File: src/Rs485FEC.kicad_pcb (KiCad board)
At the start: 2 copper layers, 24 x 27.9 mm, 20 parts, among them J1 B4B-XH-A, P1 105444-0001, Q1 DMP3099L-13, U1 FT232RL, U2 SP485E

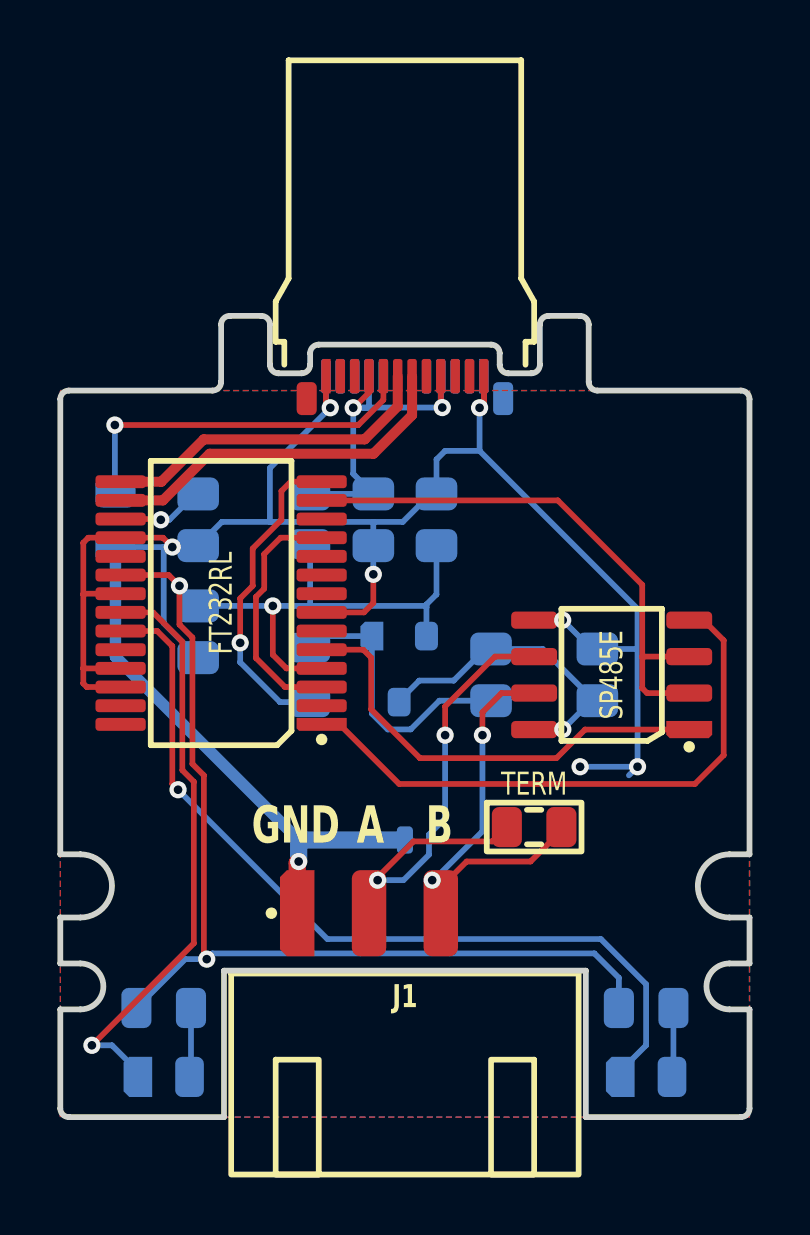
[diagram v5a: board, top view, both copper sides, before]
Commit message: Added PWREN pullup and moved LED 5V to switched
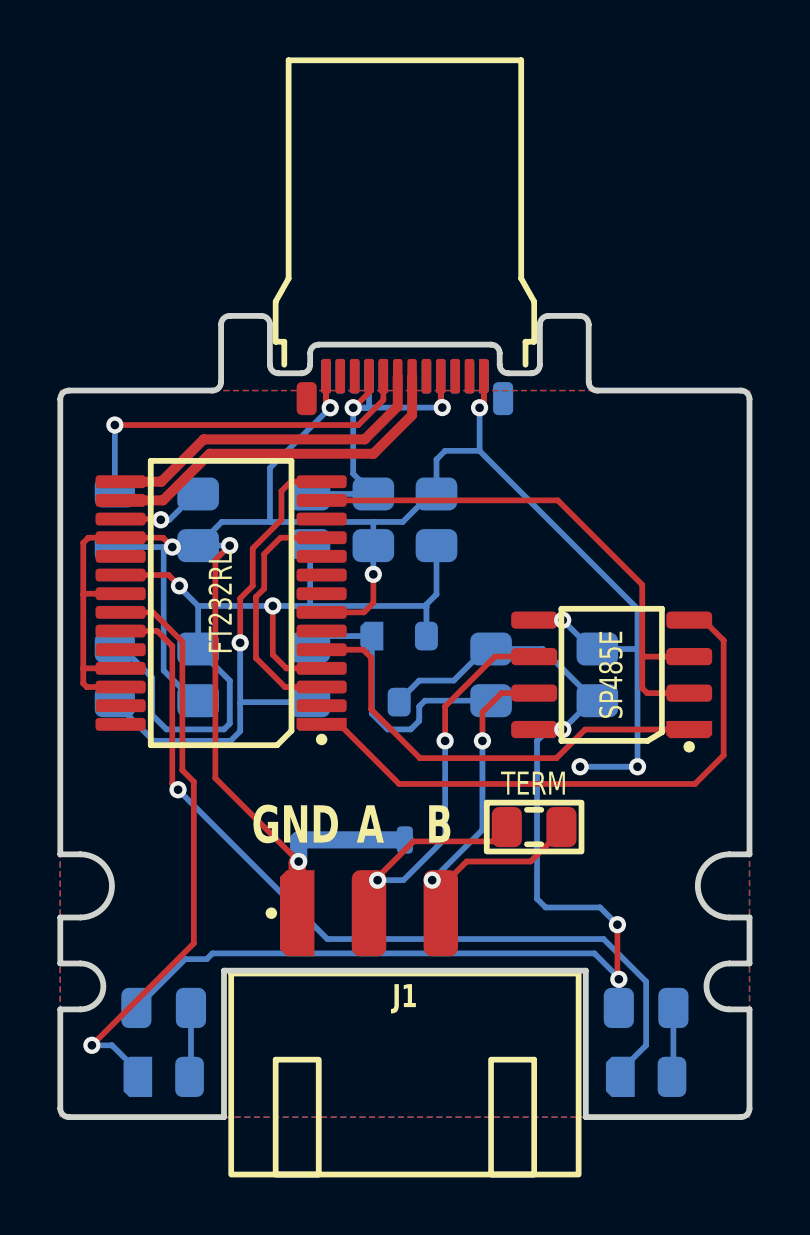
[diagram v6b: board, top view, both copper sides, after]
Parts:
- added R6: 10K, Medo64:R (0805), B.Cu at (21.9, 32.5)
- moved C2 1.50 mm to (24.8, 32.5)
- renumbered R4 to R2, R5 to R3, R6 to R4, R7 to R5
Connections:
- R2 pad 1: 5V -> 5V_SW
- R3 pad 1: 5V -> 5V_SW
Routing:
- net 5V_SW: track 10.2 -> 40.9 mm, vias 1 -> 3
- net 5V: track 52.6 -> 30.5 mm, vias 3 -> 2
- net PWREN#: track 11.3 -> 18.0 mm
- net GND: track 87.5 -> 89.2 mm, vias 8 -> 9

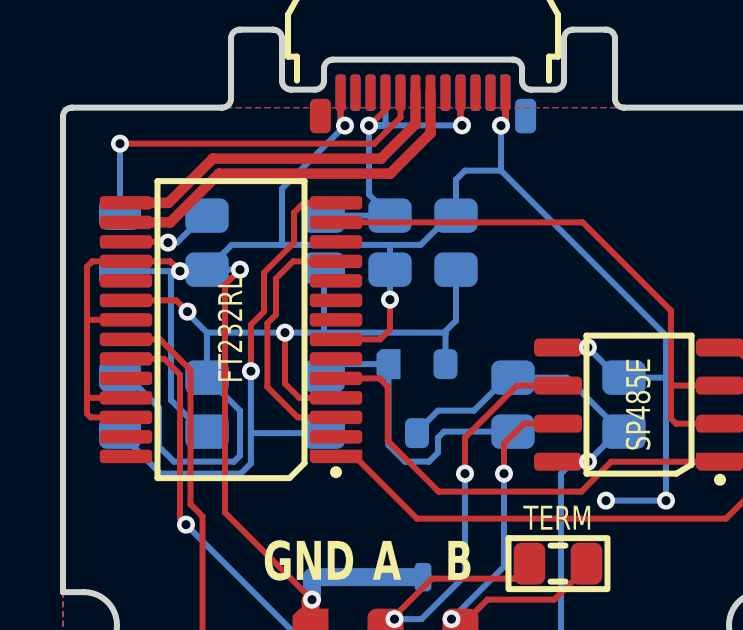
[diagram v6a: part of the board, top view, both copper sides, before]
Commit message: Removed internal RTS/CTS connection
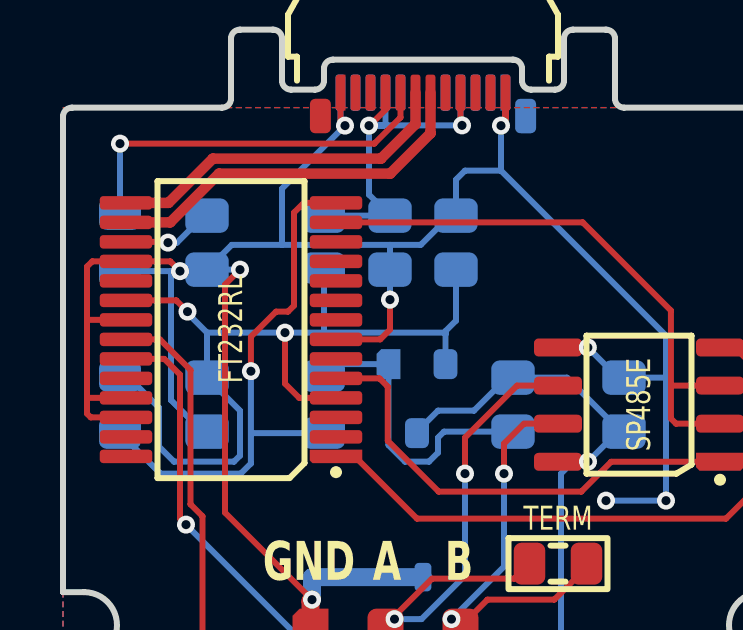
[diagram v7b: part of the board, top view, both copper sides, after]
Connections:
- U1 pad 11: RTS_CTS -> (no net)
- U1 pad 3: RTS_CTS -> (no net)
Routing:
- net RTS_CTS: track 8.68 -> 0.00 mm
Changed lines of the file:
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@@
   (net 18 "B")
   (net 19 "TXDEN")
-  (net 20 "RTS_CTS")
   (footprint "Medo64:R (0805)" (layer "F.Cu")
     (at 36.5 37.8)
@@
       (thermal_bridge_angle 45))
     (pad "3" smd roundrect (at -3.5 -2.925 180) (size 1.75 0.45) (layers "F.Cu" "F.Paste" "F.Mask") (roundrect_rratio 0.25)
-      (net 20 "RTS_CTS") (thermal_bridge_angle 45))
+      (thermal_bridge_angle 45))
     (pad "4" smd roundrect (at -3.5 -2.275 180) (size 1.75 0.45) (layers "F.Cu" "F.Paste" "F.Mask") (roundrect_rratio 0.25)
       (net 3 "5V") (thermal_bridge_angle 45))
@@
       (thermal_bridge_angle 45))
     (pad "11" smd roundrect (at -3.5 2.275 180) (size 1.75 0.45) (layers "F.Cu" "F.Paste" "F.Mask") (roundrect_rratio 0.25)
-      (net 20 "RTS_CTS") (thermal_bridge_angle 45))
+      (thermal_bridge_angle 45))
     (pad "12" smd roundrect (at -3.5 2.925 180) (size 1.75 0.45) (layers "F.Cu" "F.Paste" "F.Mask") (roundrect_rratio 0.25)
       (thermal_bridge_angle 45))
@@
   (segment (start 30.85 31.15) (end 30.85 33.85) (width 0.2) (layer "B.Cu") (net 15))
   (segment (start 32.5 33.6) (end 32.7 33.4) (width 0.2) (layer "B.Cu") (net 15))
-  (segment (start 26.7 28.1) (end 26.7 29.4) (width 0.2) (layer "F.Cu") (net 16))
-  (segment (start 27.7 27.1) (end 26.7 28.1) (width 0.2) (layer "F.Cu") (net 16))
-  (segment (start 27.7 26.1) (end 27.7 27.1) (width 0.2) (layer "F.Cu") (net 16))
+  (segment (start 27.7 29.2) (end 27.5 29.4) (width 0.2) (layer "F.Cu") (net 16))
+  (segment (start 27.1 29.4) (end 26.263909 30.236091) (width 0.2) (layer "F.Cu") (net 16))
+  (segment (start 27.5 29.4) (end 27.1 29.4) (width 0.2) (layer "F.Cu") (net 16))
   (segment (start 29.1 25.775) (end 28.025 25.775) (width 0.2) (layer "F.Cu") (net 16))
-  (segment (start 26.263909 29.836091) (end 26.263909 31.386091) (width 0.2) (layer "F.Cu") (net 16))
+  (segment (start 27.7 26.1) (end 27.7 29.2) (width 0.2) (layer "F.Cu") (net 16))
   (segment (start 28.025 25.775) (end 27.7 26.1) (width 0.2) (layer "F.Cu") (net 16))
-  (segment (start 26.7 29.4) (end 26.263909 29.836091) (width 0.2) (layer "F.Cu") (net 16))
+  (segment (start 26.263909 30.236091) (end 26.263909 31.386091) (width 0.2) (layer "F.Cu") (net 16))
   (via (at 26.263909 31.386091) (size 0.6) (drill 0.3) (layers "F.Cu" "B.Cu") (net 16))
   (segment (start 25.927818 34.8) (end 26.263909 34.463909) (width 0.2) (layer "B.Cu") (net 16))
@@
   (segment (start 29.1 26.425) (end 37.325 26.425) (width 0.2) (layer "F.Cu") (net 19))
   (segment (start 40.435 33.135) (end 40.265 32.965) (width 0.2) (layer "F.Cu") (net 19))
-  (segment (start 27.825 32.925) (end 26.813909 31.913909) (width 0.2) (layer "F.Cu") (net 20))
-  (segment (start 26.813909 29.786091) (end 27.1 29.5) (width 0.2) (layer "F.Cu") (net 20))
-  (segment (start 27.669974 27.725) (end 29.1 27.725) (width 0.2) (layer "F.Cu") (net 20))
-  (segment (start 27.1 28.294974) (end 27.669974 27.725) (width 0.2) (layer "F.Cu") (net 20))
-  (segment (start 29.1 32.925) (end 27.825 32.925) (width 0.2) (layer "F.Cu") (net 20))
-  (segment (start 26.813909 31.913909) (end 26.813909 29.786091) (width 0.2) (layer "F.Cu") (net 20))
-  (segment (start 27.1 29.5) (end 27.1 28.294974) (width 0.2) (layer "F.Cu") (net 20))
   (zone (net 7) (net_name "GND") (layers "F&B.Cu") (hatch edge 0.5)
     (connect_pads (clearance 0.2))

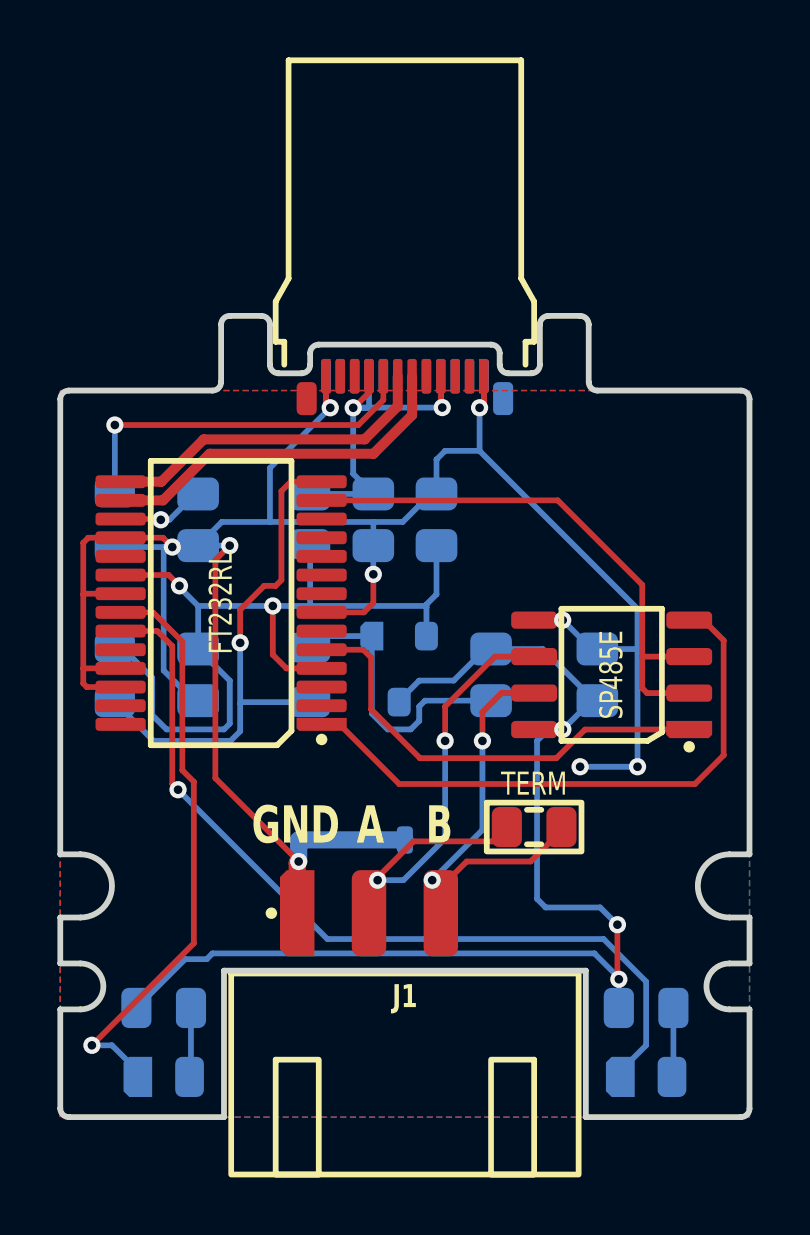
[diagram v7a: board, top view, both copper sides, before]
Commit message: Updated connector to solder all 4 pins
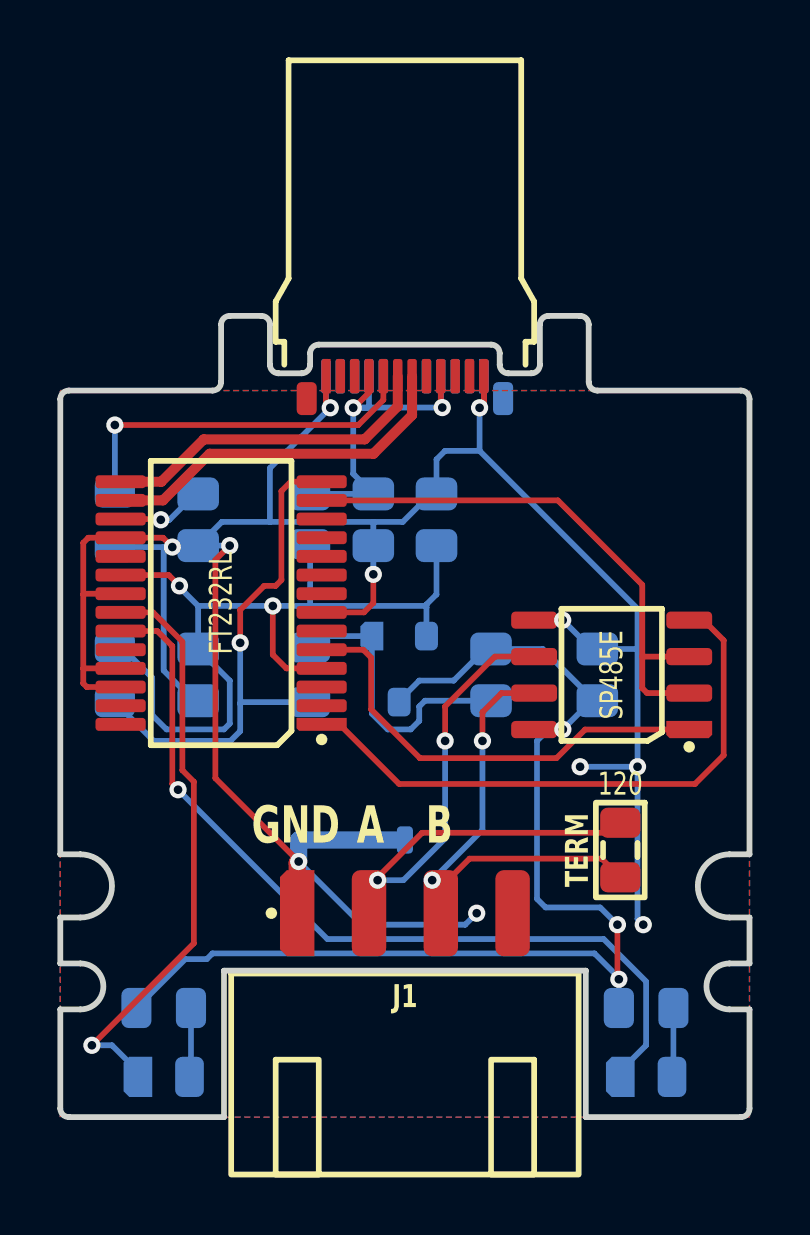
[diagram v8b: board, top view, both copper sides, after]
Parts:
- R1: value TERM -> 120
- moved R1 3.10 mm to (39.5, 38.6), turned to -90 degrees
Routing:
- net GND: track 89.2 -> 102.0 mm, vias 9 -> 11
- net A: track 17.1 -> 21.2 mm
- net B: track 13.9 -> 15.8 mm
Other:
- board text added: "TERM"
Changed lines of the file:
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@@
   (net 19 "TXDEN")
   (footprint "Medo64:R (0805)" (layer "F.Cu")
-    (at 36.5 37.8)
+    (at 39.5 38.6 -90)
     (tags "RESC2013X70N")
     (attr smd)
-    (fp_text reference "R1" (at 0 -1.6) (layer "F.SilkS") hide
+    (fp_text reference "R1" (at 0 -1.6 90) (layer "F.SilkS") hide
         (effects (font (size 0.8 0.6) (thickness 0.15)))
     )
-    (fp_text value "TERM" (at 0 -1.5 180) (layer "F.SilkS")
+    (fp_text value "120" (at -2.3 0 180) (layer "F.SilkS")
         (effects (font (size 0.8 0.6) (thickness 0.15)))
     )
@@
     (fp_rect (start -1 -0.625) (end 1 0.625)
       (stroke (width 0.01) (type dash_dot)) (fill none) (layer "F.Fab"))
-    (pad "1" smd roundrect (at -0.95 0) (size 1.05 1.4) (layers "F.Cu" "F.Paste" "F.Mask") (roundrect_rratio 0.25)
+    (pad "1" smd roundrect (at -0.95 0 270) (size 1.05 1.4) (layers "F.Cu" "F.Paste" "F.Mask") (roundrect_rratio 0.25)
       (net 17 "A") (thermal_bridge_angle 45))
-    (pad "2" smd roundrect (at 0.95 0) (size 1.05 1.4) (layers "F.Cu" "F.Paste" "F.Mask") (roundrect_rratio 0.25)
+    (pad "2" smd roundrect (at 0.95 0 270) (size 1.05 1.4) (layers "F.Cu" "F.Paste" "F.Mask") (roundrect_rratio 0.25)
       (net 18 "B") (thermal_bridge_angle 45))
     (model ":KICAD7_3DMODEL_DIR:Resistor_SMD.3dshapes/R_0805_2012Metric.step"
@@
         (effects (font (size 0.13 0.07) (thickness 0.01) bold))
     )
+    (fp_text user "A" (at -1.25 -1.65) (layer "Cmts.User" knockout)
+        (effects (font (size 0.13 0.07) (thickness 0.01) bold))
+    )
     (fp_text user "B" (at 1.25 -1.65) (layer "Cmts.User" knockout)
         (effects (font (size 0.13 0.07) (thickness 0.01) bold))
     )
-    (fp_text user "A" (at -1.25 -1.65) (layer "Cmts.User" knockout)
+    (fp_text user "N/C" (at 3.75 -1.65) (layer "Cmts.User" knockout)
         (effects (font (size 0.13 0.07) (thickness 0.01) bold))
     )
@@
     (pad "3" smd roundrect (at 1.25 0) (size 1.2 3) (layers "F.Cu" "F.Paste" "F.Mask") (roundrect_rratio 0.25)
       (net 18 "B"))
+    (pad "4" smd roundrect (at 3.75 0) (size 1.2 3) (layers "F.Cu" "F.Paste" "F.Mask") (roundrect_rratio 0.25))
     (model ":KICAD7_3DMODEL_DIR:Connector_JST.3dshapes/JST_XH_B4B-XH-A_1x04_P2.50mm_Vertical.step"
       (offset (xyz -3.75 -2 0.25))
@@
   (gr_text "A" (at 30.8 38.5) (layer "F.SilkS" knockout)
     (effects (font (size 1.3 0.9) (thickness 0.15) bold) (justify bottom))
+  )
+  (gr_text "TERM" (at 38 38.6 90) (layer "F.SilkS")
+    (effects (font (size 0.8 0.6) (thickness 0.15) bold))
   )
   (segment (start 31.25 22.927808) (end 30.377808 23.8) (width 0.2) (layer "F.Cu") (net 1))
@@
   (via (at 30.9 29) (size 0.6) (drill 0.3) (layers "F.Cu" "B.Cu") (net 7))
   (via (at 40.1 35.7) (size 0.6) (drill 0.3) (layers "F.Cu" "B.Cu") (free) (net 7))
+  (via (at 40.3 41.2) (size 0.6) (drill 0.3) (layers "F.Cu" "B.Cu") (free) (net 7))
+  (via (at 34.5 40.8) (size 0.6) (drill 0.3) (layers "F.Cu" "B.Cu") (free) (net 7))
   (via (at 34.6 23.2) (size 0.6) (drill 0.3) (layers "F.Cu" "B.Cu") (net 7))
   (segment (start 40.1 31.6) (end 40.1 35.7) (width 0.2) (layer "B.Cu") (net 7))
   (segment (start 24.65 33.4) (end 23.6 32.35) (width 0.2) (layer "B.Cu") (net 7))
   (segment (start 33.4 24.7) (end 34.6 24.7) (width 0.2) (layer "B.Cu") (net 7))
+  (segment (start 30.5 41.2) (end 34.1 41.2) (width 0.2) (layer "B.Cu") (net 7))
   (segment (start 29.4 23.2) (end 27.3 25.3) (width 0.2) (layer "B.Cu") (net 7))
   (segment (start 40.1 30.2) (end 40.1 31.6) (width 0.2) (layer "B.Cu") (net 7))
+  (segment (start 40.1 41) (end 40.3 41.2) (width 0.2) (layer "B.Cu") (net 7))
+  (segment (start 40.1 35.7) (end 40.1 41) (width 0.2) (layer "B.Cu") (net 7))
   (segment (start 30.9 27.175) (end 31.925 27.175) (width 0.2) (layer "B.Cu") (net 7))
   (segment (start 38.1 35.7) (end 40.1 35.7) (width 0.2) (layer "B.Cu") (net 7))
@@
   (segment (start 24.15 28.05) (end 23.9 28.05) (width 0.2) (layer "B.Cu") (net 7))
   (segment (start 23.6 28.05) (end 23.9 28.05) (width 0.2) (layer "B.Cu") (net 7))
+  (segment (start 28.3 39) (end 30.5 41.2) (width 0.2) (layer "B.Cu") (net 7))
   (segment (start 27.3 25.3) (end 27.3 27.175) (width 0.2) (layer "B.Cu") (net 7))
   (segment (start 25.625 27.175) (end 27.3 27.175) (width 0.2) (layer "B.Cu") (net 7))
@@
   (segment (start 30.9 29) (end 30.9 28) (width 0.2) (layer "B.Cu") (net 7))
   (segment (start 24.8 28) (end 25.625 27.175) (width 0.2) (layer "B.Cu") (net 7))
+  (segment (start 34.1 41.2) (end 34.5 40.8) (width 0.2) (layer "B.Cu") (net 7))
   (segment (start 33.25 22.1) (end 33.25 23.15) (width 0.2) (layer "F.Cu") (net 8))
   (segment (start 30.220236 23.19999) (end 30.2 23.19999) (width 0.2) (layer "F.Cu") (net 8))
@@
   (segment (start 33.4 33.6) (end 33.4 34.8) (width 0.2) (layer "F.Cu") (net 17))
   (segment (start 35.135 31.865) (end 33.4 33.6) (width 0.2) (layer "F.Cu") (net 17))
+  (segment (start 31.05 39.55) (end 32.6 38) (width 0.2) (layer "F.Cu") (net 17))
+  (segment (start 32.6 38) (end 39.15 38) (width 0.2) (layer "F.Cu") (net 17))
   (segment (start 36.5 31.865) (end 35.135 31.865) (width 0.2) (layer "F.Cu") (net 17))
-  (segment (start 35.05 38.3) (end 35.55 37.8) (width 0.2) (layer "F.Cu") (net 17))
-  (segment (start 31.05 39.55) (end 32.3 38.3) (width 0.2) (layer "F.Cu") (net 17))
-  (segment (start 32.3 38.3) (end 35.05 38.3) (width 0.2) (layer "F.Cu") (net 17))
+  (segment (start 39.15 38) (end 39.5 37.65) (width 0.2) (layer "F.Cu") (net 17))
   (via (at 31.049975 39.65) (size 0.6) (drill 0.3) (layers "F.Cu" "B.Cu") (net 17))
   (via (at 33.4 34.8) (size 0.6) (drill 0.3) (layers "F.Cu" "B.Cu") (net 17))
@@
   (segment (start 31.049975 39.65) (end 31.95 39.65) (width 0.2) (layer "B.Cu") (net 17))
   (segment (start 36.5 33.135) (end 35.365 33.135) (width 0.2) (layer "F.Cu") (net 18))
-  (segment (start 33.500014 39.649986) (end 34.15 39) (width 0.2) (layer "F.Cu") (net 18))
+  (segment (start 33.500014 39.649986) (end 34.25 38.9) (width 0.2) (layer "F.Cu") (net 18))
   (segment (start 34.7 33.8) (end 34.7 34.799996) (width 0.2) (layer "F.Cu") (net 18))
-  (segment (start 34.15 39) (end 36.375 39) (width 0.2) (layer "F.Cu") (net 18))
-  (segment (start 36.375 39) (end 37.45 37.925) (width 0.2) (layer "F.Cu") (net 18))
+  (segment (start 38.85 38.9) (end 39.5 39.55) (width 0.2) (layer "F.Cu") (net 18))
+  (segment (start 34.25 38.9) (end 38.85 38.9) (width 0.2) (layer "F.Cu") (net 18))
   (segment (start 35.365 33.135) (end 34.7 33.8) (width 0.2) (layer "F.Cu") (net 18))
   (via (at 34.7 34.799996) (size 0.6) (drill 0.3) (layers "F.Cu" "B.Cu") (net 18))
